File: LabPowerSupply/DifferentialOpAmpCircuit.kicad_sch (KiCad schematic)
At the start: 14 parts

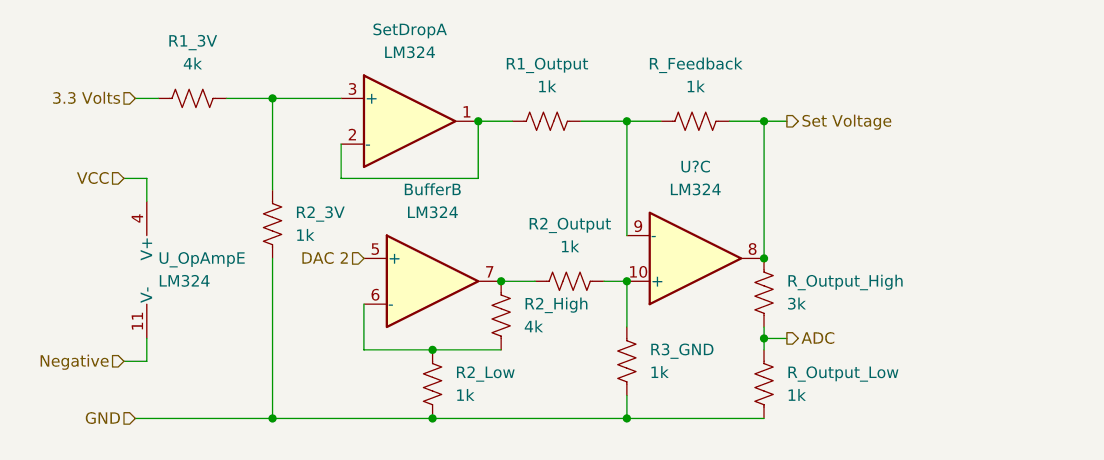
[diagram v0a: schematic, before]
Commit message: Finished first pass on the schematic
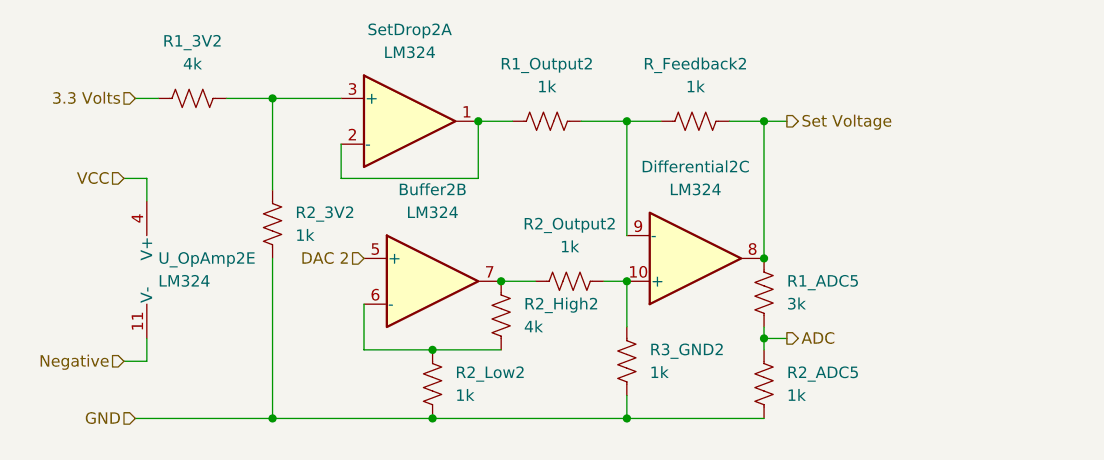
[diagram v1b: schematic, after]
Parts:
- removed R_Output_High: 3k, Resistor_SMD:R_1210_3225Metric, symbol Device:R_US
- removed R_Output_Low: 1k, Resistor_SMD:R_1210_3225Metric, symbol Device:R_US
- added R1_ADC5: 3k, Resistor_SMD:R_1210_3225Metric, symbol Device:R_US
- added R2_ADC5: 1k, Resistor_SMD:R_1210_3225Metric, symbol Device:R_US
- gave numbers to parts that had none: 1
- renumbered Buffer to Buffer2, R1_3V to R1_3V2, R1_Output to R1_Output2, R2_3V to R2_3V2, R2_High to R2_High2, R2_Low to R2_Low2, R2_Output to R2_Output2, R3_GND to R3_GND2, R_Feedback to R_Feedback2, SetDrop to SetDrop2, U_OpAmp to U_OpAmp2
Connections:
- net ADC: now also R1_ADC5.2, R2_ADC5.1
- net GND: now also R2_ADC5.2
- net Set Voltage: now also R1_ADC5.1

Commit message: started PCB
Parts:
- renumbered Buffer2 to OpAmp2, SetDrop2 to OpAmp2, Differential2 to OpAmp2
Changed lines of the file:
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@@
   (symbol (lib_id "Amplifier_Operational:LM324") (at 129.54 104.14 0) (unit 2)
     (in_bom yes) (on_board yes) (fields_autoplaced)
-    (property "Reference" "Buffer2" (id 0) (at 129.54 93.98 0))
+    (property "Reference" "OpAmp2" (id 0) (at 129.54 93.98 0))
     (property "Value" "LM324" (id 1) (at 129.54 96.52 0))
     (property "Footprint" "Package_SO:SOIC-14_3.9x8.7mm_P1.27mm" (id 2) (at 128.27 101.6 0)
@@
   (symbol (lib_id "Amplifier_Operational:LM324") (at 127 86.36 0) (unit 1)
     (in_bom yes) (on_board yes) (fields_autoplaced)
-    (property "Reference" "SetDrop2" (id 0) (at 127 76.2 0))
+    (property "Reference" "OpAmp2" (id 0) (at 127 76.2 0))
     (property "Value" "LM324" (id 1) (at 127 78.74 0))
     (property "Footprint" "Package_SO:SOIC-14_3.9x8.7mm_P1.27mm" (id 2) (at 125.73 83.82 0)
@@
   (symbol (lib_id "Amplifier_Operational:LM324") (at 158.75 101.6 0) (mirror x) (unit 3)
     (in_bom yes) (on_board yes) (fields_autoplaced)
-    (property "Reference" "Differential2" (id 0) (at 158.75 91.44 0))
+    (property "Reference" "OpAmp2" (id 0) (at 158.75 91.44 0))
     (property "Value" "LM324" (id 1) (at 158.75 93.98 0))
     (property "Footprint" "Package_SO:SOIC-14_3.9x8.7mm_P1.27mm" (id 2) (at 157.48 104.14 0)

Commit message: more work
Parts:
- OpAmp1: renamed from U_OpAmp2; footprint Package_SO:SOIC-14_3.9x8.7mm_P1.27mm -> Package_DIP:DIP-14_W7.62mm
- OpAmp1: renamed from OpAmp2; footprint Package_SO:SOIC-14_3.9x8.7mm_P1.27mm -> Package_DIP:DIP-14_W7.62mm
- renumbered R2_ADC5 to R10_OA1, R1_3V2 to R1_OA1, R2_3V2 to R2_OA1, R1_Output2 to R3_OA1, R2_Output2 to R4_OA1, R2_High2 to R5_OA1, R2_Low2 to R6_OA1, R_Feedback2 to R7_OA1, R3_GND2 to R8_OA1, R1_ADC5 to R9_OA1
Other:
- moved on the sheet: OpAmp1E
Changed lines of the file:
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@@
     (stroke (width 0) (type default) (color 0 0 0 0))
   )
-  (wire (pts (xy 95.25 92.71) (xy 97.79 92.71))
+  (wire (pts (xy 96.52 93.98) (xy 99.06 93.98))
     (stroke (width 0) (type default) (color 0 0 0 0))
   )
@@
     (stroke (width 0) (type default) (color 0 0 0 0))
   )
-  (wire (pts (xy 97.79 92.71) (xy 97.79 95.25))
+  (wire (pts (xy 99.06 93.98) (xy 99.06 96.52))
     (stroke (width 0) (type default) (color 0 0 0 0))
   )
@@
     (stroke (width 0) (type default) (color 0 0 0 0))
   )
-  (wire (pts (xy 97.79 113.03) (xy 95.25 113.03))
+  (wire (pts (xy 99.06 114.3) (xy 96.52 114.3))
     (stroke (width 0) (type default) (color 0 0 0 0))
   )
@@
     (stroke (width 0) (type default) (color 0 0 0 0))
   )
-  (wire (pts (xy 97.79 110.49) (xy 97.79 113.03))
+  (wire (pts (xy 99.06 111.76) (xy 99.06 114.3))
     (stroke (width 0) (type default) (color 0 0 0 0))
   )
@@
     (effects (font (size 1.27 1.27)) (justify right))
   )
-  (hierarchical_label "Negative" (shape input) (at 95.25 113.03 180)
-    (effects (font (size 1.27 1.27)) (justify right))
-  )
-  (hierarchical_label "VCC" (shape input) (at 95.25 92.71 180)
+  (hierarchical_label "Negative" (shape input) (at 96.52 114.3 180)
+    (effects (font (size 1.27 1.27)) (justify right))
+  )
+  (hierarchical_label "VCC" (shape input) (at 96.52 93.98 180)
     (effects (font (size 1.27 1.27)) (justify right))
   )
@@
   (symbol (lib_id "Device:R_US") (at 166.37 105.41 0) (unit 1)
     (in_bom yes) (on_board yes) (fields_autoplaced)
-    (property "Reference" "R1_ADC5" (id 0) (at 168.91 104.1399 0)
+    (property "Reference" "R9_OA1" (id 0) (at 168.91 104.1399 0)
       (effects (font (size 1.27 1.27)) (justify left))
     )
@@
     (pin "2")
   )
-  (symbol (lib_id "Amplifier_Operational:LM324") (at 100.33 102.87 0) (unit 5)
-    (in_bom yes) (on_board yes) (fields_autoplaced)
-    (property "Reference" "U_OpAmp2" (id 0) (at 99.06 101.5999 0)
-      (effects (font (size 1.27 1.27)) (justify left))
-    )
-    (property "Value" "LM324" (id 1) (at 99.06 104.1399 0)
-      (effects (font (size 1.27 1.27)) (justify left))
-    )
-    (property "Footprint" "Package_SO:SOIC-14_3.9x8.7mm_P1.27mm" (id 2) (at 99.06 100.33 0)
-      (effects (font (size 1.27 1.27)) hide)
-    )
-    (property "Datasheet" "http://www.ti.com/lit/ds/symlink/lm2902-n.pdf" (id 3) (at 101.6 97.79 0)
+  (symbol (lib_id "Amplifier_Operational:LM324") (at 101.6 104.14 0) (unit 5)
+    (in_bom yes) (on_board yes) (fields_autoplaced)
+    (property "Reference" "OpAmp1" (id 0) (at 100.33 102.8699 0)
+      (effects (font (size 1.27 1.27)) (justify left))
+    )
+    (property "Value" "LM324" (id 1) (at 100.33 105.4099 0)
+      (effects (font (size 1.27 1.27)) (justify left))
+    )
+    (property "Footprint" "Package_DIP:DIP-14_W7.62mm" (id 2) (at 100.33 101.6 0)
+      (effects (font (size 1.27 1.27)) hide)
+    )
+    (property "Datasheet" "http://www.ti.com/lit/ds/symlink/lm2902-n.pdf" (id 3) (at 102.87 99.06 0)
       (effects (font (size 1.27 1.27)) hide)
     )
@@
   (symbol (lib_id "Device:R_US") (at 142.24 86.36 90) (unit 1)
     (in_bom yes) (on_board yes) (fields_autoplaced)
-    (property "Reference" "R1_Output2" (id 0) (at 142.24 80.01 90))
+    (property "Reference" "R3_OA1" (id 0) (at 142.24 80.01 90))
     (property "Value" "1k" (id 1) (at 142.24 82.55 90))
     (property "Footprint" "Resistor_SMD:R_1210_3225Metric" (id 2) (at 142.494 85.344 90)
@@
   (symbol (lib_id "Device:R_US") (at 102.87 83.82 90) (unit 1)
     (in_bom yes) (on_board yes) (fields_autoplaced)
-    (property "Reference" "R1_3V2" (id 0) (at 102.87 77.47 90))
+    (property "Reference" "R1_OA1" (id 0) (at 102.87 77.47 90))
     (property "Value" "4k" (id 1) (at 102.87 80.01 90))
     (property "Footprint" "Resistor_SMD:R_1210_3225Metric" (id 2) (at 103.124 82.804 90)
@@
   (symbol (lib_id "Device:R_US") (at 111.76 97.79 0) (unit 1)
     (in_bom yes) (on_board yes) (fields_autoplaced)
-    (property "Reference" "R2_3V2" (id 0) (at 114.3 96.5199 0)
+    (property "Reference" "R2_OA1" (id 0) (at 114.3 96.5199 0)
       (effects (font (size 1.27 1.27)) (justify left))
     )
@@
   (symbol (lib_id "Device:R_US") (at 129.54 115.57 0) (unit 1)
     (in_bom yes) (on_board yes) (fields_autoplaced)
-    (property "Reference" "R2_Low2" (id 0) (at 132.08 114.2999 0)
+    (property "Reference" "R6_OA1" (id 0) (at 132.08 114.2999 0)
       (effects (font (size 1.27 1.27)) (justify left))
     )
@@
   (symbol (lib_id "Device:R_US") (at 144.78 104.14 90) (unit 1)
     (in_bom yes) (on_board yes) (fields_autoplaced)
-    (property "Reference" "R2_Output2" (id 0) (at 144.78 97.79 90))
+    (property "Reference" "R4_OA1" (id 0) (at 144.78 97.79 90))
     (property "Value" "1k" (id 1) (at 144.78 100.33 90))
     (property "Footprint" "Resistor_SMD:R_1210_3225Metric" (id 2) (at 145.034 103.124 90)
@@
   (symbol (lib_id "Amplifier_Operational:LM324") (at 129.54 104.14 0) (unit 2)
     (in_bom yes) (on_board yes) (fields_autoplaced)
-    (property "Reference" "OpAmp2" (id 0) (at 129.54 93.98 0))
+    (property "Reference" "OpAmp1" (id 0) (at 129.54 93.98 0))
     (property "Value" "LM324" (id 1) (at 129.54 96.52 0))
-    (property "Footprint" "Package_SO:SOIC-14_3.9x8.7mm_P1.27mm" (id 2) (at 128.27 101.6 0)
+    (property "Footprint" "Package_DIP:DIP-14_W7.62mm" (id 2) (at 128.27 101.6 0)
       (effects (font (size 1.27 1.27)) hide)
     )
@@
   (symbol (lib_id "Amplifier_Operational:LM324") (at 127 86.36 0) (unit 1)
     (in_bom yes) (on_board yes) (fields_autoplaced)
-    (property "Reference" "OpAmp2" (id 0) (at 127 76.2 0))
+    (property "Reference" "OpAmp1" (id 0) (at 127 76.2 0))
     (property "Value" "LM324" (id 1) (at 127 78.74 0))
-    (property "Footprint" "Package_SO:SOIC-14_3.9x8.7mm_P1.27mm" (id 2) (at 125.73 83.82 0)
+    (property "Footprint" "Package_DIP:DIP-14_W7.62mm" (id 2) (at 125.73 83.82 0)
       (effects (font (size 1.27 1.27)) hide)
     )
@@
   (symbol (lib_id "Device:R_US") (at 166.37 115.57 0) (unit 1)
     (in_bom yes) (on_board yes) (fields_autoplaced)
-    (property "Reference" "R2_ADC5" (id 0) (at 168.91 114.2999 0)
+    (property "Reference" "R10_OA1" (id 0) (at 168.91 114.2999 0)
       (effects (font (size 1.27 1.27)) (justify left))
     )
@@
   (symbol (lib_id "Device:R_US") (at 158.75 86.36 90) (unit 1)
     (in_bom yes) (on_board yes) (fields_autoplaced)
-    (property "Reference" "R_Feedback2" (id 0) (at 158.75 80.01 90))
+    (property "Reference" "R7_OA1" (id 0) (at 158.75 80.01 90))
     (property "Value" "1k" (id 1) (at 158.75 82.55 90))
     (property "Footprint" "Resistor_SMD:R_1210_3225Metric" (id 2) (at 159.004 85.344 90)
@@
   (symbol (lib_id "Device:R_US") (at 151.13 113.03 0) (unit 1)
     (in_bom yes) (on_board yes) (fields_autoplaced)
-    (property "Reference" "R3_GND2" (id 0) (at 153.67 111.7599 0)
+    (property "Reference" "R8_OA1" (id 0) (at 153.67 111.7599 0)
       (effects (font (size 1.27 1.27)) (justify left))
     )
@@
   (symbol (lib_id "Device:R_US") (at 137.16 107.95 0) (unit 1)
     (in_bom yes) (on_board yes) (fields_autoplaced)
-    (property "Reference" "R2_High2" (id 0) (at 139.7 106.6799 0)
+    (property "Reference" "R5_OA1" (id 0) (at 139.7 106.6799 0)
       (effects (font (size 1.27 1.27)) (justify left))
     )
@@
   (symbol (lib_id "Amplifier_Operational:LM324") (at 158.75 101.6 0) (mirror x) (unit 3)
     (in_bom yes) (on_board yes) (fields_autoplaced)
-    (property "Reference" "OpAmp2" (id 0) (at 158.75 91.44 0))
+    (property "Reference" "OpAmp1" (id 0) (at 158.75 91.44 0))
     (property "Value" "LM324" (id 1) (at 158.75 93.98 0))
-    (property "Footprint" "Package_SO:SOIC-14_3.9x8.7mm_P1.27mm" (id 2) (at 157.48 104.14 0)
-      (effects (font (size 1.27 1.27)) hide)
-    )
+    (property "Footprint" "Package_DIP:DIP-14_W7.62mm" (id 2) (at 157.48 104.14 0)
+      (effects (font (size 1.27 1.27)) hide)
+    )

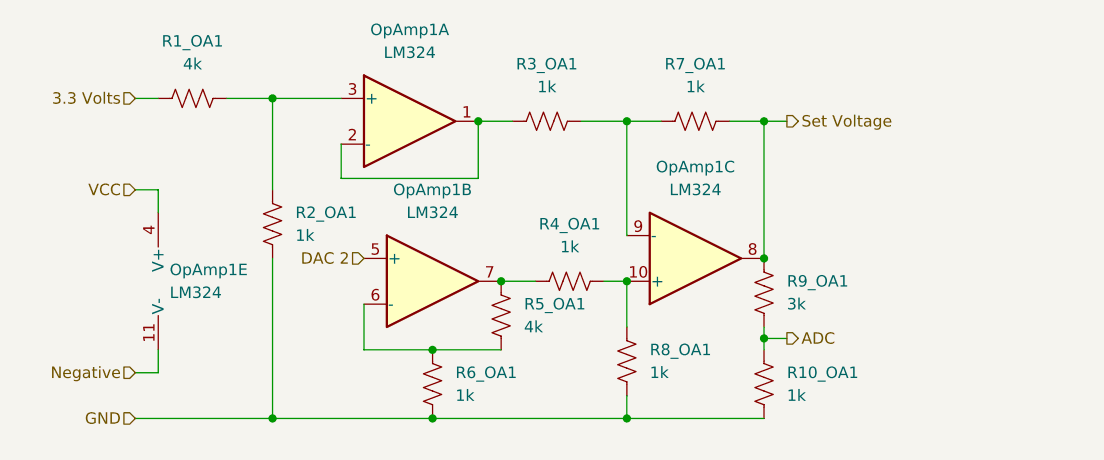
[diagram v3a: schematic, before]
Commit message: Resistor footprints changed to 0603
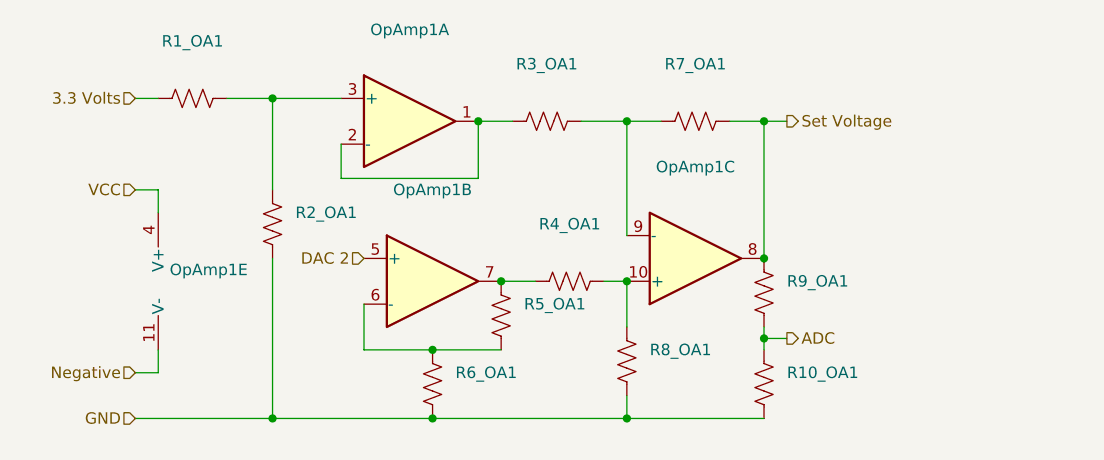
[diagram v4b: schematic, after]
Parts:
- OpAmp1: value LM324 -> (none); footprint Package_DIP:DIP-14_W7.62mm -> (none)
- R10_OA1, R2_OA1, R3_OA1, R4_OA1, R6_OA1, R7_OA1, R8_OA1: value 1k -> (none); footprint Resistor_SMD:R_1210_3225Metric -> (none)
- R1_OA1, R5_OA1: value 4k -> (none); footprint Resistor_SMD:R_1210_3225Metric -> (none)
- R9_OA1: value 3k -> (none); footprint Resistor_SMD:R_1210_3225Metric -> (none)
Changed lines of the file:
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@@
       (effects (font (size 1.27 1.27)) (justify left))
     )
-    (property "Value" "3k" (id 1) (at 168.91 106.6799 0)
-      (effects (font (size 1.27 1.27)) (justify left))
-    )
-    (property "Footprint" "Resistor_SMD:R_1210_3225Metric" (id 2) (at 167.386 105.664 90)
+    (property "Value" "" (id 1) (at 168.91 106.6799 0)
+      (effects (font (size 1.27 1.27)) (justify left))
+    )
+    (property "Footprint" "" (id 2) (at 167.386 105.664 90)
       (effects (font (size 1.27 1.27)) hide)
     )
@@
       (effects (font (size 1.27 1.27)) (justify left))
     )
-    (property "Value" "LM324" (id 1) (at 100.33 105.4099 0)
-      (effects (font (size 1.27 1.27)) (justify left))
-    )
-    (property "Footprint" "Package_DIP:DIP-14_W7.62mm" (id 2) (at 100.33 101.6 0)
+    (property "Value" "" (id 1) (at 100.33 105.4099 0)
+      (effects (font (size 1.27 1.27)) (justify left))
+    )
+    (property "Footprint" "" (id 2) (at 100.33 101.6 0)
       (effects (font (size 1.27 1.27)) hide)
     )
@@
     (in_bom yes) (on_board yes) (fields_autoplaced)
     (property "Reference" "R3_OA1" (id 0) (at 142.24 80.01 90))
-    (property "Value" "1k" (id 1) (at 142.24 82.55 90))
-    (property "Footprint" "Resistor_SMD:R_1210_3225Metric" (id 2) (at 142.494 85.344 90)
+    (property "Value" "" (id 1) (at 142.24 82.55 90))
+    (property "Footprint" "" (id 2) (at 142.494 85.344 90)
       (effects (font (size 1.27 1.27)) hide)
     )
@@
     (in_bom yes) (on_board yes) (fields_autoplaced)
     (property "Reference" "R1_OA1" (id 0) (at 102.87 77.47 90))
-    (property "Value" "4k" (id 1) (at 102.87 80.01 90))
-    (property "Footprint" "Resistor_SMD:R_1210_3225Metric" (id 2) (at 103.124 82.804 90)
+    (property "Value" "" (id 1) (at 102.87 80.01 90))
+    (property "Footprint" "" (id 2) (at 103.124 82.804 90)
       (effects (font (size 1.27 1.27)) hide)
     )
@@
       (effects (font (size 1.27 1.27)) (justify left))
     )
-    (property "Value" "1k" (id 1) (at 114.3 99.0599 0)
-      (effects (font (size 1.27 1.27)) (justify left))
-    )
-    (property "Footprint" "Resistor_SMD:R_1210_3225Metric" (id 2) (at 112.776 98.044 90)
+    (property "Value" "" (id 1) (at 114.3 99.0599 0)
+      (effects (font (size 1.27 1.27)) (justify left))
+    )
+    (property "Footprint" "" (id 2) (at 112.776 98.044 90)
       (effects (font (size 1.27 1.27)) hide)
     )
@@
       (effects (font (size 1.27 1.27)) (justify left))
     )
-    (property "Value" "1k" (id 1) (at 132.08 116.8399 0)
-      (effects (font (size 1.27 1.27)) (justify left))
-    )
-    (property "Footprint" "Resistor_SMD:R_1210_3225Metric" (id 2) (at 130.556 115.824 90)
+    (property "Value" "" (id 1) (at 132.08 116.8399 0)
+      (effects (font (size 1.27 1.27)) (justify left))
+    )
+    (property "Footprint" "" (id 2) (at 130.556 115.824 90)
       (effects (font (size 1.27 1.27)) hide)
     )
@@
     (in_bom yes) (on_board yes) (fields_autoplaced)
     (property "Reference" "R4_OA1" (id 0) (at 144.78 97.79 90))
-    (property "Value" "1k" (id 1) (at 144.78 100.33 90))
-    (property "Footprint" "Resistor_SMD:R_1210_3225Metric" (id 2) (at 145.034 103.124 90)
+    (property "Value" "" (id 1) (at 144.78 100.33 90))
+    (property "Footprint" "" (id 2) (at 145.034 103.124 90)
       (effects (font (size 1.27 1.27)) hide)
     )
@@
     (in_bom yes) (on_board yes) (fields_autoplaced)
     (property "Reference" "OpAmp1" (id 0) (at 129.54 93.98 0))
-    (property "Value" "LM324" (id 1) (at 129.54 96.52 0))
-    (property "Footprint" "Package_DIP:DIP-14_W7.62mm" (id 2) (at 128.27 101.6 0)
+    (property "Value" "" (id 1) (at 129.54 96.52 0))
+    (property "Footprint" "" (id 2) (at 128.27 101.6 0)
       (effects (font (size 1.27 1.27)) hide)
     )
@@
     (in_bom yes) (on_board yes) (fields_autoplaced)
     (property "Reference" "OpAmp1" (id 0) (at 127 76.2 0))
-    (property "Value" "LM324" (id 1) (at 127 78.74 0))
-    (property "Footprint" "Package_DIP:DIP-14_W7.62mm" (id 2) (at 125.73 83.82 0)
+    (property "Value" "" (id 1) (at 127 78.74 0))
+    (property "Footprint" "" (id 2) (at 125.73 83.82 0)
       (effects (font (size 1.27 1.27)) hide)
     )
@@
       (effects (font (size 1.27 1.27)) (justify left))
     )
-    (property "Value" "1k" (id 1) (at 168.91 116.8399 0)
-      (effects (font (size 1.27 1.27)) (justify left))
-    )
-    (property "Footprint" "Resistor_SMD:R_1210_3225Metric" (id 2) (at 167.386 115.824 90)
+    (property "Value" "" (id 1) (at 168.91 116.8399 0)
+      (effects (font (size 1.27 1.27)) (justify left))
+    )
+    (property "Footprint" "" (id 2) (at 167.386 115.824 90)
       (effects (font (size 1.27 1.27)) hide)
     )
@@
     (in_bom yes) (on_board yes) (fields_autoplaced)
     (property "Reference" "R7_OA1" (id 0) (at 158.75 80.01 90))
-    (property "Value" "1k" (id 1) (at 158.75 82.55 90))
-    (property "Footprint" "Resistor_SMD:R_1210_3225Metric" (id 2) (at 159.004 85.344 90)
+    (property "Value" "" (id 1) (at 158.75 82.55 90))
+    (property "Footprint" "" (id 2) (at 159.004 85.344 90)
       (effects (font (size 1.27 1.27)) hide)
     )
@@
       (effects (font (size 1.27 1.27)) (justify left))
     )
-    (property "Value" "1k" (id 1) (at 153.67 114.2999 0)
-      (effects (font (size 1.27 1.27)) (justify left))
-    )
-    (property "Footprint" "Resistor_SMD:R_1210_3225Metric" (id 2) (at 152.146 113.284 90)
+    (property "Value" "" (id 1) (at 153.67 114.2999 0)
+      (effects (font (size 1.27 1.27)) (justify left))
+    )
+    (property "Footprint" "" (id 2) (at 152.146 113.284 90)
       (effects (font (size 1.27 1.27)) hide)
     )
@@
       (effects (font (size 1.27 1.27)) (justify left))
     )
-    (property "Value" "4k" (id 1) (at 139.7 109.2199 0)
-      (effects (font (size 1.27 1.27)) (justify left))
-    )
-    (property "Footprint" "Resistor_SMD:R_1210_3225Metric" (id 2) (at 138.176 108.204 90)
+    (property "Value" "" (id 1) (at 139.7 109.2199 0)
+      (effects (font (size 1.27 1.27)) (justify left))
+    )
+    (property "Footprint" "" (id 2) (at 138.176 108.204 90)
       (effects (font (size 1.27 1.27)) hide)
     )
@@
     (in_bom yes) (on_board yes) (fields_autoplaced)
     (property "Reference" "OpAmp1" (id 0) (at 158.75 91.44 0))
-    (property "Value" "LM324" (id 1) (at 158.75 93.98 0))
-    (property "Footprint" "Package_DIP:DIP-14_W7.62mm" (id 2) (at 157.48 104.14 0)
-      (effects (font (size 1.27 1.27)) hide)
-    )
+    (property "Value" "" (id 1) (at 158.75 93.98 0))
+    (property "Footprint" "" (id 2) (at 157.48 104.14 0)
+      (effects (font (size 1.27 1.27)) hide)
+    )
